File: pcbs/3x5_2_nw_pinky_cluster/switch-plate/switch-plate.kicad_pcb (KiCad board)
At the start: 2 copper layers, 131.1 x 89.8 mm, 21 parts, among them SW1 Choc, SW10 Choc, SW11 Choc, SW12 Choc, SW13 Choc, SW14 Choc, SW15 Choc, SW16 Choc, SW17 Choc, SW2 Choc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

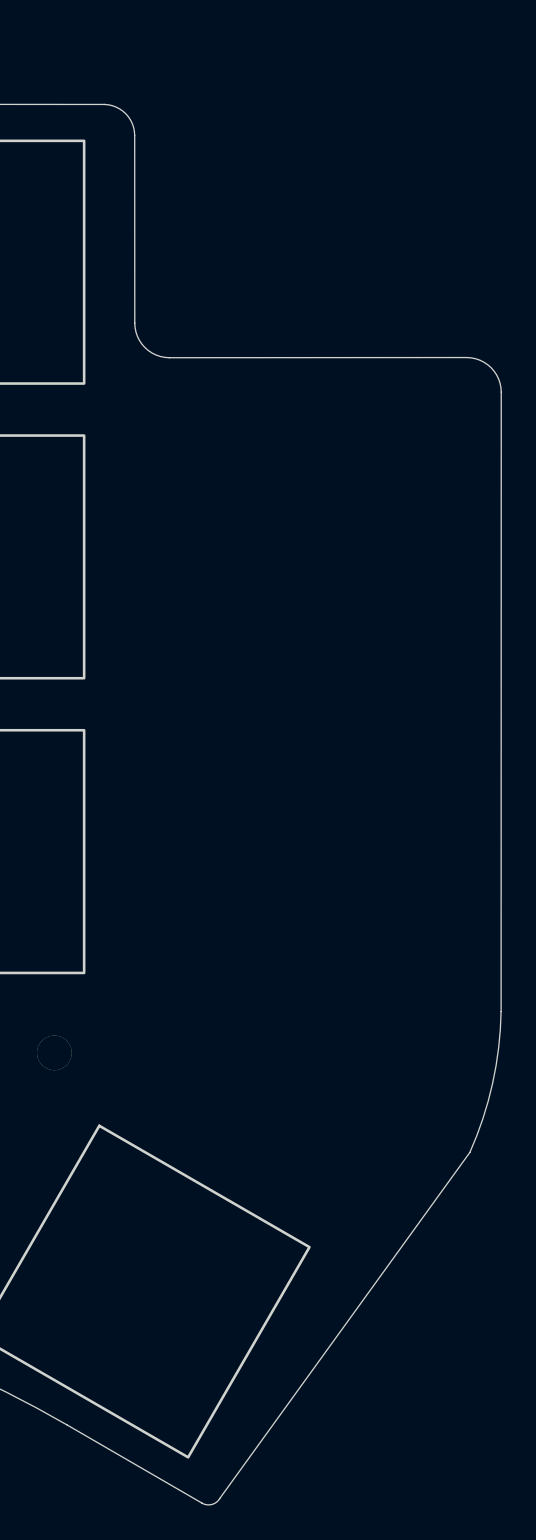
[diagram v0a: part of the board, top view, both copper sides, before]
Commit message: removing gerbers/ folders, only keeping gerbers.zip
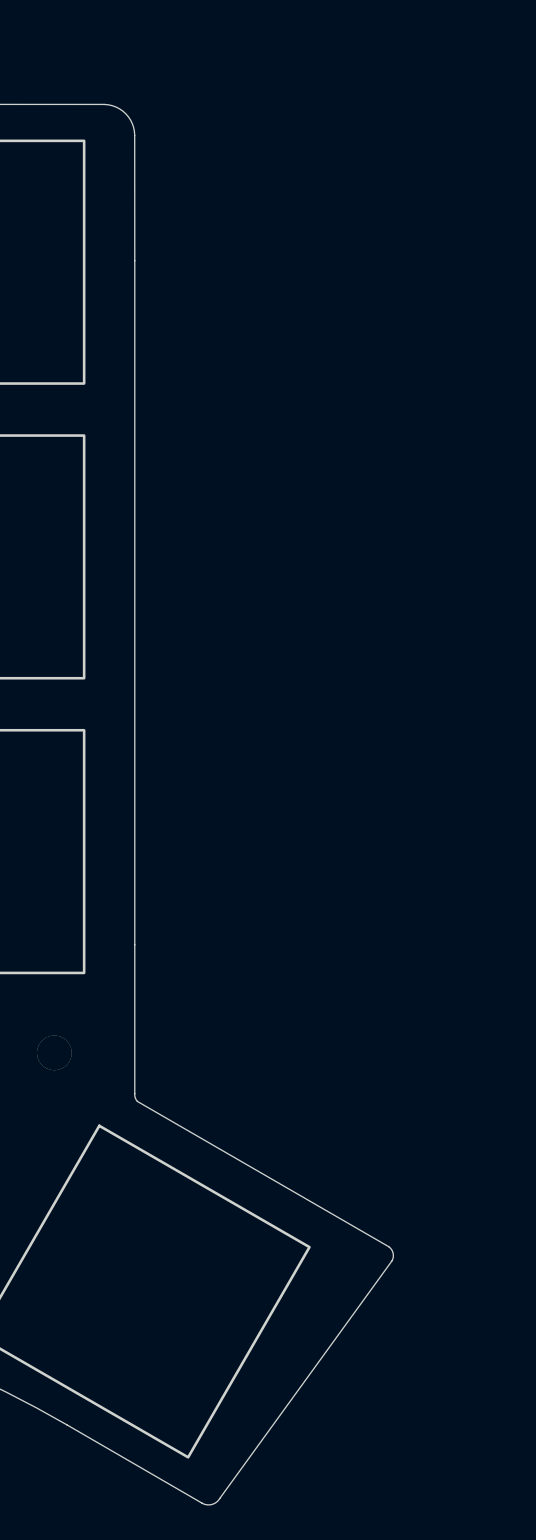
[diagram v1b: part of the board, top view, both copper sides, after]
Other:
- board size 131.1 x 89.8 mm -> 124.9 x 89.8 mm
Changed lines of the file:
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@@
   (title_block
     (title "Altenswoop")
-    (date "2023-08-10")
+    (date "2023-08-23")
     (rev "0.6.1")
     (company "SuperFola")
@@
   (gr_line (start 61.188834 79.86901) (end 61.183001 92.962834)
     (stroke (width 0.05) (type solid)) (layer "Edge.Cuts"))
-  (gr_line (start 153.15 81.749331) (end 153.145111 70.933883)
-    (stroke (width 0.05) (type solid)) (layer "Edge.Cuts"))
-  (gr_line (start 174.29 85.74) (end 174.281568 121.466832)
-    (stroke (width 0.05) (type solid)) (layer "Edge.Cuts"))
   (gr_line (start 133.616117 66.633883) (end 118.540222 66.661837)
     (stroke (width 0.05) (type solid)) (layer "Edge.Cuts"))
@@
   (gr_arc (start 136.116117 69.133883) (mid 135.232234 68.767766) (end 134.866117 67.883883)
     (stroke (width 0.05) (type solid)) (layer "Edge.Cuts"))
+  (gr_line (start 153.15 78.15) (end 153.150253 117.617143)
+    (stroke (width 0.05) (type solid)) (layer "Edge.Cuts"))
   (gr_line (start 79.547715 67.826168) (end 79.543548 76.357158)
     (stroke (width 0.05) (type solid)) (layer "Edge.Cuts"))
@@
   (gr_arc (start 97.595381 61.858541) (mid 98.138076 60.621651) (end 99.389516 60.11343)
     (stroke (width 0.05) (type solid)) (layer "Edge.Cuts"))
+  (gr_line (start 158.055405 149.550557) (end 167.990425 135.844628)
+    (stroke (width 0.05) (type solid)) (layer "Edge.Cuts"))
   (gr_arc (start 122.285509 117.800624) (mid 122.570287 117.933532) (end 122.686243 118.225623)
     (stroke (width 0.05) (type default)) (layer "Edge.Cuts"))
@@
   (gr_arc (start 115.05 60.1) (mid 116.286898 60.642691) (end 116.795111 61.894135)
     (stroke (width 0.05) (type solid)) (layer "Edge.Cuts"))
-  (gr_arc (start 155.149984 83.749464) (mid 153.735753 83.163601) (end 153.15 81.749331)
-    (stroke (width 0.05) (type solid)) (layer "Edge.Cuts"))
-  (gr_arc (start 151.4 69.139748) (mid 152.63689 69.682443) (end 153.145111 70.933883)
-    (stroke (width 0.05) (type solid)) (layer "Edge.Cuts"))
   (gr_line (start 107.96051 118.201358) (end 107.942708 134.510435)
     (stroke (width 0.05) (type default)) (layer "Edge.Cuts"))
   (gr_line (start 43.2 96.453802) (end 43.2 112)
     (stroke (width 0.05) (type solid)) (layer "Edge.Cuts"))
-  (gr_arc (start 174.281567 121.466832) (mid 173.789865 125.619716) (end 172.48064 129.591384)
-    (stroke (width 0.05) (type solid)) (layer "Edge.Cuts"))
   (gr_arc (start 122.735508 134.54989) (mid 122.602545 134.83461) (end 122.310509 134.950624)
     (stroke (width 0.05) (type default)) (layer "Edge.Cuts"))
   (gr_line (start 151.4 69.139748) (end 136.116117 69.133883)
     (stroke (width 0.05) (type solid)) (layer "Edge.Cuts"))
+  (gr_arc (start 153.300001 126.65) (mid 153.178818 126.440394) (end 153.150001 126.2)
+    (stroke (width 0.05) (type default)) (layer "Edge.Cuts"))
   (gr_arc (start 79.543548 76.357158) (mid 79.000006 77.600024) (end 77.745029 78.114927)
     (stroke (width 0.05) (type solid)) (layer "Edge.Cuts"))
@@
   (gr_arc (start 158.055405 149.550557) (mid 157.600001 149.900002) (end 157.030886 149.825076)
     (stroke (width 0.05) (type solid)) (layer "Edge.Cuts"))
+  (gr_arc (start 151.4 69.139748) (mid 152.636864 69.682462) (end 153.145111 70.933883)
+    (stroke (width 0.05) (type solid)) (layer "Edge.Cuts"))
+  (gr_line (start 153.15 78.15) (end 153.145111 70.933883)
+    (stroke (width 0.05) (type solid)) (layer "Edge.Cuts"))
+  (gr_line (start 167.797034 135.029526) (end 153.300001 126.65)
+    (stroke (width 0.05) (type default)) (layer "Edge.Cuts"))
   (gr_line (start 108.343442 134.935434) (end 122.310509 134.950624)
     (stroke (width 0.05) (type default)) (layer "Edge.Cuts"))
@@
   (gr_arc (start 107.96051 118.201358) (mid 108.093426 117.916589) (end 108.385509 117.800624)
     (stroke (width 0.05) (type default)) (layer "Edge.Cuts"))
+  (gr_arc (start 167.797034 135.029526) (mid 168.049975 135.400006) (end 167.990425 135.844628)
+    (stroke (width 0.05) (type default)) (layer "Edge.Cuts"))
   (gr_line (start 108.385509 117.800624) (end 122.285509 117.800624)
     (stroke (width 0.05) (type default)) (layer "Edge.Cuts"))
-  (gr_arc (start 172.290016 83.739867) (mid 173.704245 84.325728) (end 174.29 85.74)
-    (stroke (width 0.05) (type solid)) (layer "Edge.Cuts"))
   (gr_arc (start 108.343442 134.935434) (mid 108.058694 134.802498) (end 107.942708 134.510435)
     (stroke (width 0.05) (type default)) (layer "Edge.Cuts"))
+  (gr_line (start 153.150253 117.617143) (end 153.15 126.2)
+    (stroke (width 0.05) (type solid)) (layer "Edge.Cuts"))
   (gr_arc (start 97.6 64.338143) (mid 97.057294 65.575) (end 95.805865 66.083254)
     (stroke (width 0.05) (type solid)) (layer "Edge.Cuts"))
   (gr_line (start 97.595381 61.858541) (end 97.6 64.338143)
     (stroke (width 0.05) (type solid)) (layer "Edge.Cuts"))
-  (gr_line (start 158.055405 149.550557) (end 172.48064 129.591384)
-    (stroke (width 0.05) (type solid)) (layer "Edge.Cuts"))
   (gr_arc (start 118.540222 66.661837) (mid 117.303351 66.119136) (end 116.795111 64.867702)
     (stroke (width 0.05) (type solid)) (layer "Edge.Cuts"))
   (gr_line (start 95.805865 66.083254) (end 81.352199 66.070992)
     (stroke (width 0.05) (type solid)) (layer "Edge.Cuts"))
-  (gr_line (start 155.149984 83.749464) (end 172.290016 83.739867)
-    (stroke (width 0.05) (type solid)) (layer "Edge.Cuts"))
   (gr_arc (start 61.183001 92.962834) (mid 60.64 94.2) (end 59.388184 94.708318)
